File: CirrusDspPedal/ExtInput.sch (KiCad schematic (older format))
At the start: 20 parts, among them J5 MonoJack2Switch, SW1 P26L-1D-RND MTL, SW2 P26L-1D-RND MTL, SW3 SW_SPST, SW4 SW_SPST, U6 MCP601-xOT

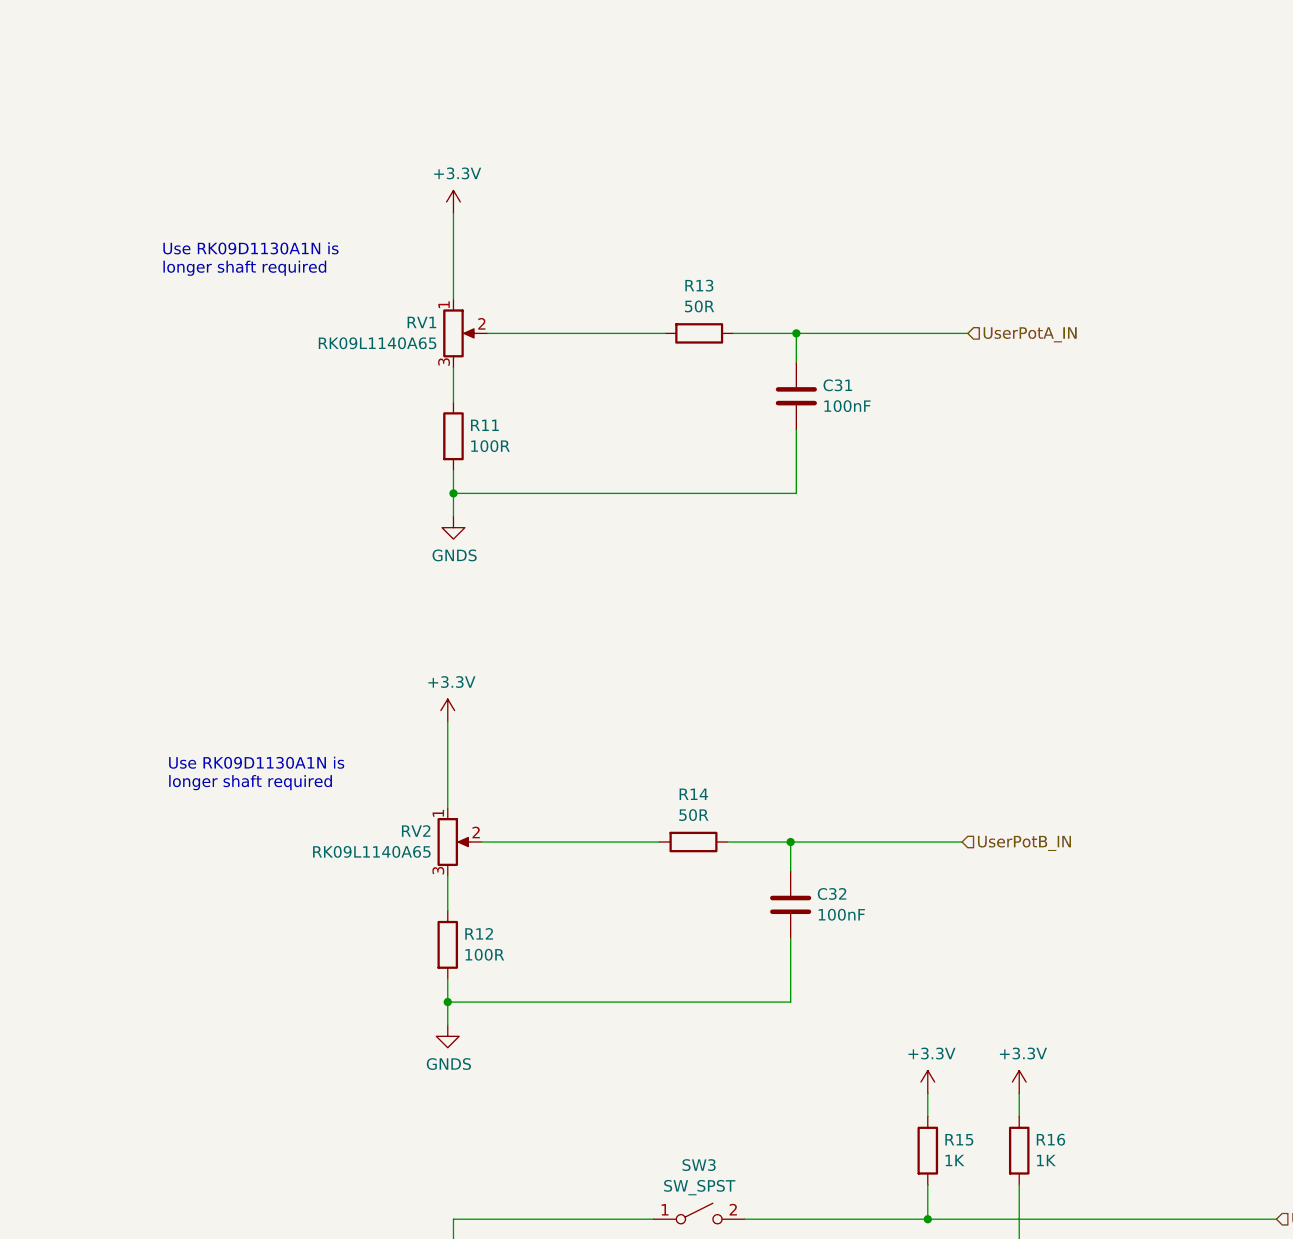
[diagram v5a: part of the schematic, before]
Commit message: Updated RevB
- Replaced analog pots with Rotary Encoders
- Added I2C connector (for OLED screen)
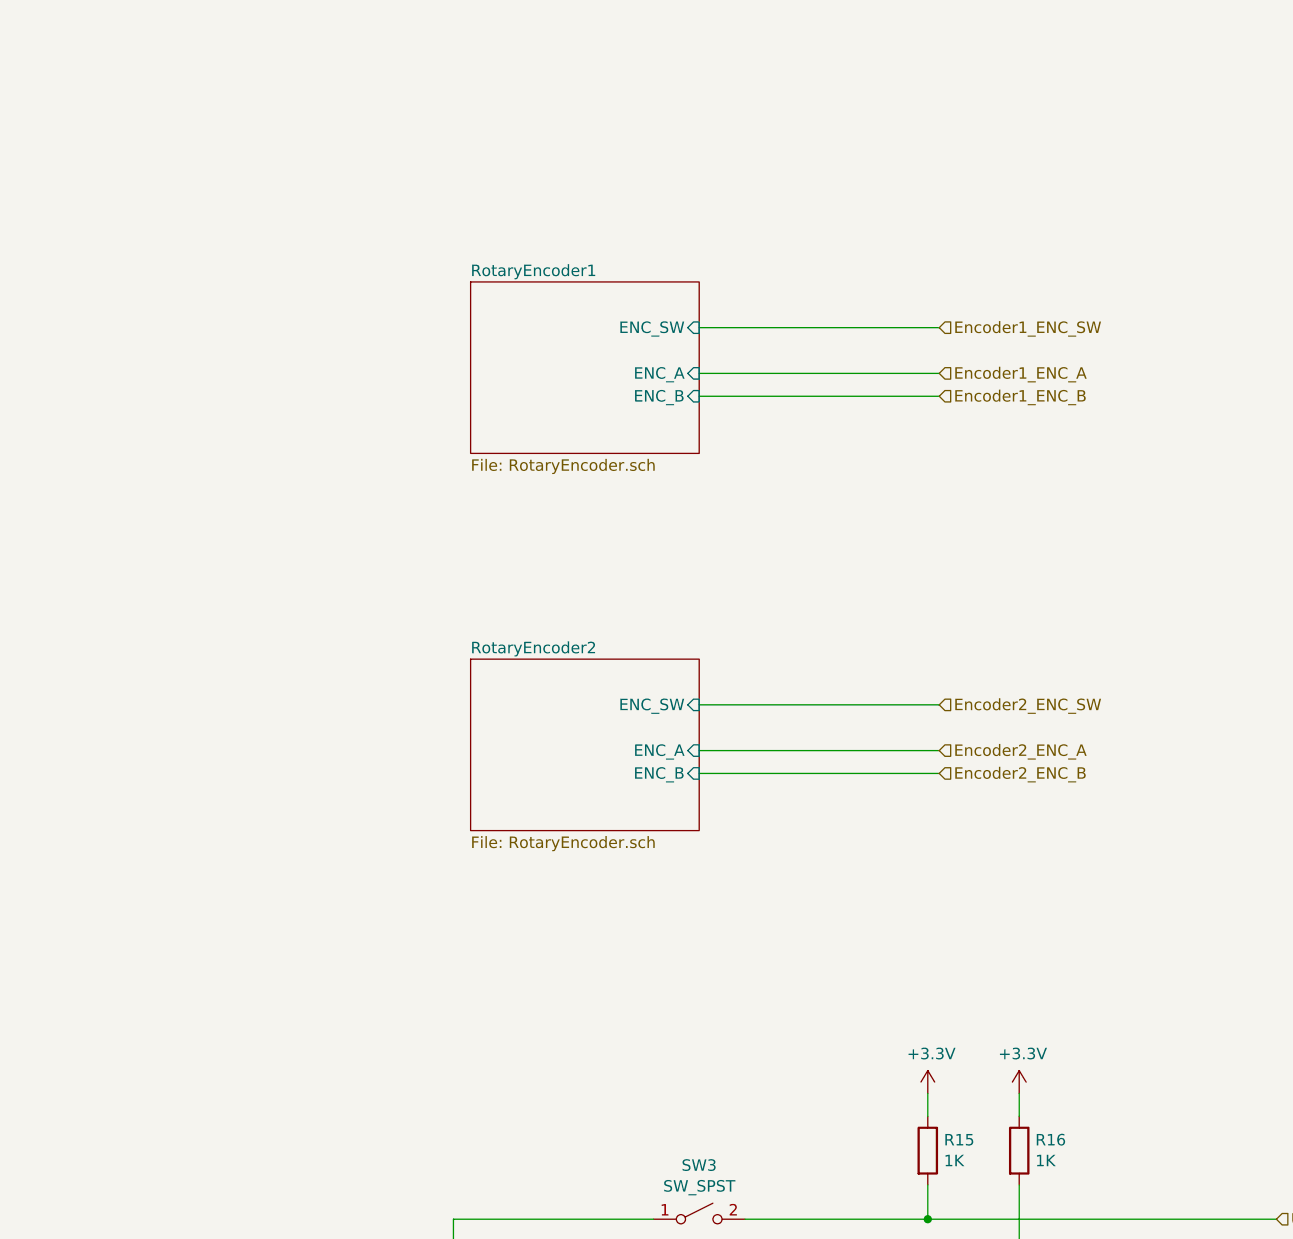
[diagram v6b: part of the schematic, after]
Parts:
- removed C31, C32: 100nF, Capacitor_SMD:C_0805_2012Metric_Pad1.15x1.40mm_HandSolder, symbol Device:C
- removed R11, R12: 100R, Resistor_SMD:R_0805_2012Metric_Pad1.15x1.40mm_HandSolder, symbol Device:R
- removed R13, R14: 50R, Resistor_SMD:R_0805_2012Metric_Pad1.15x1.40mm_HandSolder, symbol Device:R
- removed RV1, RV2: RK09L1140A65, Potentiometer_THT:Potentiometer_Alps_RK09L_Single_Vertical, symbol Device:R_POT
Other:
- note removed: "Use RK09D1130A1N is \nlonger shaft required"
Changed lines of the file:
@@
 $Descr A3 11693 16535 portrait
 encoding utf-8
-Sheet 9 10
+Sheet 9 12
 Title ""
 Date ""
@@
 	6075 7150 6075 7050
 $Comp
-L Device:R_POT RV1
-U 1 1 5F8FDBD5
-P 4775 9575
-F 0 "RV1" H 4706 9621 50  0000 R CNN
-F 1 " RK09L1140A65" H 4706 9530 50  0000 R CNN
-F 2 "Potentiometer_THT:Potentiometer_Alps_RK09L_Single_Vertical" H 4775 9575 50  0001 C CNN
-F 3 "https://tech.alpsalpine.com/prod/e/pdf/potentiometer/rotarypotentiometers/rk09l/rk09l.pdf" H 4775 9575 50  0001 C CNN
-	1    4775 9575
-	1    0    0    -1
-$EndComp
-Wire Wire Line
-	4775 9425 4775 9050
-$Comp
-L power:+3.3V #PWR06
-U 1 1 5F900058
-P 4775 9050
-F 0 "#PWR06" H 4775 8900 50  0001 C CNN
-F 1 "+3.3V" H 4790 9223 50  0000 C CNN
-F 2 "" H 4775 9050 50  0001 C CNN
-F 3 "" H 4775 9050 50  0001 C CNN
-	1    4775 9050
-	1    0    0    -1
-$EndComp
-$Comp
-L Device:R R11
-U 1 1 5F90026E
-P 4775 10025
-F 0 "R11" H 4845 10071 50  0000 L CNN
-F 1 "100R" H 4845 9980 50  0000 L CNN
-F 2 "Resistor_SMD:R_0805_2012Metric_Pad1.15x1.40mm_HandSolder" V 4705 10025 50  0001 C CNN
-F 3 "~" H 4775 10025 50  0001 C CNN
-	1    4775 10025
-	1    0    0    -1
-$EndComp
-Wire Wire Line
-	4775 9875 4775 9725
-Wire Wire Line
-	4775 10175 4775 10275
-$Comp
-L power:GNDS #PWR07
-U 1 1 5F9015F0
-P 4775 10375
-F 0 "#PWR07" H 4775 10125 50  0001 C CNN
-F 1 "GNDS" H 4780 10202 50  0000 C CNN
-F 2 "" H 4775 10375 50  0001 C CNN
-F 3 "" H 4775 10375 50  0001 C CNN
-	1    4775 10375
-	1    0    0    -1
-$EndComp
-Wire Wire Line
-	4925 9575 5700 9575
-Text HLabel 7025 9575 2    50   Input ~ 0
-UserPotA_IN
-$Comp
-L Device:R R13
-U 1 1 5F901F3D
-P 5850 9575
-F 0 "R13" V 5643 9575 50  0000 C CNN
-F 1 "50R" V 5734 9575 50  0000 C CNN
-F 2 "Resistor_SMD:R_0805_2012Metric_Pad1.15x1.40mm_HandSolder" V 5780 9575 50  0001 C CNN
-F 3 "~" H 5850 9575 50  0001 C CNN
-	1    5850 9575
-	0    1    1    0
-$EndComp
-Wire Wire Line
-	6000 9575 6275 9575
-$Comp
-L Device:C C?
-U 1 1 5F9025AC
-P 6275 9850
-AR Path="/5F834C36/5F9025AC" Ref="C?"  Part="1"
-AR Path="/5F898CA5/5F9025AC" Ref="C31"  Part="1"
-F 0 "C31" H 6160 9804 50  0000 R CNN
-F 1 "100nF" H 6160 9895 50  0000 R CNN
-F 2 "Capacitor_SMD:C_0805_2012Metric_Pad1.15x1.40mm_HandSolder" H 6313 9700 50  0001 C CNN
-F 3 "~" H 6275 9850 50  0001 C CNN
-	1    6275 9850
-	-1   0    0    1
-$EndComp
-Wire Wire Line
-	6275 9700 6275 9575
-Connection ~ 6275 9575
-Wire Wire Line
-	6275 9575 7025 9575
-Wire Wire Line
-	6275 10000 6275 10275
-Wire Wire Line
-	6275 10275 4775 10275
-Connection ~ 4775 10275
-Wire Wire Line
-	4775 10275 4775 10375
-$Comp
-L Device:R_POT RV2
-U 1 1 5F908FDA
-P 4750 11800
-F 0 "RV2" H 4681 11846 50  0000 R CNN
-F 1 " RK09L1140A65" H 4681 11755 50  0000 R CNN
-F 2 "Potentiometer_THT:Potentiometer_Alps_RK09L_Single_Vertical" H 4750 11800 50  0001 C CNN
-F 3 "https://tech.alpsalpine.com/prod/e/pdf/potentiometer/rotarypotentiometers/rk09l/rk09l.pdf" H 4750 11800 50  0001 C CNN
-	1    4750 11800
-	1    0    0    -1
-$EndComp
-Wire Wire Line
-	4750 11650 4750 11275
-$Comp
-L power:+3.3V #PWR08
-U 1 1 5F908FE1
-P 4750 11275
-F 0 "#PWR08" H 4750 11125 50  0001 C CNN
-F 1 "+3.3V" H 4765 11448 50  0000 C CNN
-F 2 "" H 4750 11275 50  0001 C CNN
-F 3 "" H 4750 11275 50  0001 C CNN
-	1    4750 11275
-	1    0    0    -1
-$EndComp
-$Comp
-L Device:R R12
-U 1 1 5F908FE7
-P 4750 12250
-F 0 "R12" H 4820 12296 50  0000 L CNN
-F 1 "100R" H 4820 12205 50  0000 L CNN
-F 2 "Resistor_SMD:R_0805_2012Metric_Pad1.15x1.40mm_HandSolder" V 4680 12250 50  0001 C CNN
-F 3 "~" H 4750 12250 50  0001 C CNN
-	1    4750 12250
-	1    0    0    -1
-$EndComp
-Wire Wire Line
-	4750 12100 4750 11950
-Wire Wire Line
-	4750 12400 4750 12500
-$Comp
-L power:GNDS #PWR09
-U 1 1 5F908FEF
-P 4750 12600
-F 0 "#PWR09" H 4750 12350 50  0001 C CNN
-F 1 "GNDS" H 4755 12427 50  0000 C CNN
-F 2 "" H 4750 12600 50  0001 C CNN
-F 3 "" H 4750 12600 50  0001 C CNN
-	1    4750 12600
-	1    0    0    -1
-$EndComp
-Wire Wire Line
-	4900 11800 5675 11800
-Text HLabel 7000 11800 2    50   Input ~ 0
-UserPotB_IN
-$Comp
-L Device:R R14
-U 1 1 5F908FF7
-P 5825 11800
-F 0 "R14" V 5618 11800 50  0000 C CNN
-F 1 "50R" V 5709 11800 50  0000 C CNN
-F 2 "Resistor_SMD:R_0805_2012Metric_Pad1.15x1.40mm_HandSolder" V 5755 11800 50  0001 C CNN
-F 3 "~" H 5825 11800 50  0001 C CNN
-	1    5825 11800
-	0    1    1    0
-$EndComp
-Wire Wire Line
-	5975 11800 6250 11800
-$Comp
-L Device:C C?
-U 1 1 5F908FFE
-P 6250 12075
-AR Path="/5F834C36/5F908FFE" Ref="C?"  Part="1"
-AR Path="/5F898CA5/5F908FFE" Ref="C32"  Part="1"
-F 0 "C32" H 6135 12029 50  0000 R CNN
-F 1 "100nF" H 6135 12120 50  0000 R CNN
-F 2 "Capacitor_SMD:C_0805_2012Metric_Pad1.15x1.40mm_HandSolder" H 6288 11925 50  0001 C CNN
-F 3 "~" H 6250 12075 50  0001 C CNN
-	1    6250 12075
-	-1   0    0    1
-$EndComp
-Wire Wire Line
-	6250 11925 6250 11800
-Connection ~ 6250 11800
-Wire Wire Line
-	6250 11800 7000 11800
-Wire Wire Line
-	6250 12225 6250 12500
-Wire Wire Line
-	6250 12500 4750 12500
-Connection ~ 4750 12500
-Wire Wire Line
-	4750 12500 4750 12600
-$Comp
 L Switch:SW_SPST SW3
 U 1 1 5F93A731
@@
 Text HLabel 8375 13875 2    50   Input ~ 0
 UserSwitchB_IN
-Text Notes 3525 11575 0    50   ~ 0
-Use RK09D1130A1N is \nlonger shaft required
-Text Notes 3500 9325 0    50   ~ 0
-Use RK09D1130A1N is \nlonger shaft required
+$Sheet
+S 4850 9350 1000 750
+U 5FAC3062
+F0 "RotaryEncoder1" 50
+F1 "RotaryEncoder.sch" 50
+F2 "ENC_B" I R 5850 9850 50
+F3 "ENC_A" I R 5850 9750 50
+F4 "ENC_SW" I R 5850 9550 50
+$EndSheet
+$Sheet
+S 4850 11000 1000 750
+U 5FAC8ACD
+F0 "RotaryEncoder2" 50
+F1 "RotaryEncoder.sch" 50
+F2 "ENC_B" I R 5850 11500 50
+F3 "ENC_A" I R 5850 11400 50
+F4 "ENC_SW" I R 5850 11200 50
+$EndSheet
+Wire Wire Line
+	5850 9550 6900 9550
+Text HLabel 6900 9550 2    50   Input ~ 0
+Encoder1_ENC_SW
+Wire Wire Line
+	5850 9750 6900 9750
+Wire Wire Line
+	5850 9850 6900 9850
+Text HLabel 6900 9750 2    50   Input ~ 0
+Encoder1_ENC_A
+Text HLabel 6900 9850 2    50   Input ~ 0
+Encoder1_ENC_B
+Wire Wire Line
+	5850 11200 6900 11200
+Text HLabel 6900 11200 2    50   Input ~ 0
+Encoder2_ENC_SW
+Wire Wire Line
+	5850 11400 6900 11400
+Wire Wire Line
+	5850 11500 6900 11500
+Text HLabel 6900 11400 2    50   Input ~ 0
+Encoder2_ENC_A
+Text HLabel 6900 11500 2    50   Input ~ 0
+Encoder2_ENC_B
 $EndSCHEMATC
